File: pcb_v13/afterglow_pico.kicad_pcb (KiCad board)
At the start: 4 copper layers, 69.4 x 88.1 mm, 88 parts, among them J1 USB_B_Micro, J2 Conn_01x02_Male, J4 Conn_02x17_Odd_Even, J5 Conn_02x17_Odd_Even, SW1 SW_Push, U1 NCP1117-3.3_SOT223, U10 74HC257, U11 74HC257, U2 RP2040, U3 SN74LVC245AN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

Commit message: Almost
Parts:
- moved R14 8.14 mm to (162.3, 64.0), turned to 180 degrees
- moved R6 1.13 mm to (155.3, 63.2)
- moved C10 0.53 mm to (159.4, 75.7)
- moved C12 0.32 mm to (154.9, 75.6)
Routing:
- net GND: track 61.7 -> 64.4 mm
- net +3V3: track 211.1 -> 213.5 mm, vias 13 -> 12
- net /QSPI_SS: track 21.4 -> 22.2 mm

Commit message: Preparations
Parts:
- added LOGO: LOGO, pcb_v13:ag_pico_logo_2, F.Cu at (152.8, 69.8)
- moved R35 2.68 mm to (200.2, 113.8)
- moved J5 2.55 mm to (187.3, 133.3)
- moved R33 2.40 mm to (200.2, 116.5)
- moved J2 0.93 mm to (184.8, 140.8)
- turned R21 to 90 degrees
- turned R22 to 90 degrees
- turned R23 to 90 degrees
- turned R24 to 90 degrees
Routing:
- net Vcc: track 305.0 -> 285.1 mm
- net /SOL4: track 0.00 -> 17.7 mm
- net /DIS2: track 0.00 -> 10.3 mm
- net /SOL2: track 4.07 -> 14.4 mm
- net /P33: track 0.00 -> 10.2 mm
- net /SOL1: track 0.00 -> 10.1 mm
- net /ZERO_CROSS: track 0.00 -> 10.0 mm
- net /DIS3: track 0.00 -> 10.0 mm
- net /DIS1: track 0.00 -> 10.0 mm
- net /SOL3: track 7.83 -> 15.6 mm
- net /LCOL: track 0.00 -> 6.67 mm
- net /GPIO3: track 0.00 -> 4.09 mm, vias 0 -> 1
- net /GPIO15: track 0.00 -> 3.28 mm, vias 0 -> 1
- net /GPIO14: track 0.00 -> 3.04 mm, vias 0 -> 1
- net /GPIO2: track 0.00 -> 2.96 mm, vias 0 -> 1
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
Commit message: More preparations
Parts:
- + 5V -: renamed from J2
- renumbered PWR_LED1 to P
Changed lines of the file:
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@@
     (property "Sheetname" "")
     (attr smd)
-    (fp_text reference "R22" (at -0.11 1.225 90) (layer "F.SilkS")
+    (fp_text reference "R22" (at 0.06 -1.05 90) (layer "F.SilkS")
       (effects (font (size 1 1) (thickness 0.15)))
     )
@@
     (property "Sheetname" "")
     (attr smd)
-    (fp_text reference "R21" (at -0.1 1.225 90) (layer "F.SilkS")
+    (fp_text reference "R21" (at 0.025 -1.1 90) (layer "F.SilkS")
       (effects (font (size 1 1) (thickness 0.15)))
     )
@@
     (property "Sheetname" "")
     (attr through_hole)
-    (fp_text reference "J2" (at 1.265 4.125) (layer "F.SilkS")
+    (fp_text reference "+ 5V -" (at 1.075 4.375) (layer "F.SilkS")
       (effects (font (size 1 1) (thickness 0.15)))
     )
@@
     (property "Sheetname" "")
     (attr smd)
-    (fp_text reference "PWR_LED1" (at -2.635 -0.075) (layer "F.SilkS")
+    (fp_text reference "P" (at -2.36 0 180) (layer "F.SilkS")
       (effects (font (size 1 1) (thickness 0.15)))
     )
@@
     (property "Sheetname" "")
     (attr smd)
-    (fp_text reference "C4" (at 2.7 0.025) (layer "F.SilkS")
+    (fp_text reference "C4" (at 2.575 0.025) (layer "F.SilkS")
       (effects (font (size 1 1) (thickness 0.15)))
     )
@@
     (property "Sheetname" "")
     (attr smd)
-    (fp_text reference "U1" (at -0.2 4.35) (layer "F.SilkS")
+    (fp_text reference "U1" (at 0.05 4.425) (layer "F.SilkS")
       (effects (font (size 1 1) (thickness 0.15)))
     )
@@
     (property "Sheetname" "")
     (attr smd)
-    (fp_text reference "D3" (at -2.575 0.15) (layer "F.SilkS")
+    (fp_text reference "D3" (at -2.475 0) (layer "F.SilkS")
       (effects (font (size 1 1) (thickness 0.15)))
     )
@@
     (effects (font (size 0.75 0.75) (thickness 0.1)))
   )
-  (gr_text "1" (at 189.4 135.75) (layer "F.SilkS")
+  (gr_text "1" (at 189.25 133.225) (layer "F.SilkS")
     (effects (font (size 0.75 0.75) (thickness 0.1)))
   )

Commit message: Even more preparations
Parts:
- moved TEST 0.38 mm to (179.1, 61.5)
- renumbered P to PWR, TEST_MODE1 to TEST
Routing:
- net GND: track 64.4 -> 65.2 mm
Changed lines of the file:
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@@
     (property "Sheetname" "")
     (attr smd)
-    (fp_text reference "P" (at -2.36 0 180) (layer "F.SilkS")
+    (fp_text reference "PWR" (at -2.71 -0.05 180) (layer "F.SilkS")
       (effects (font (size 1 1) (thickness 0.15)))
     )
@@
   )
   (footprint "Pin_Headers:Pin_Header_Straight_1x02_Pitch2.54mm" (layer "F.Cu")
-    (at 178.78 61.65 90)
+    (at 179.1 61.45 90)
     (descr "Through hole straight pin header, 1x02, 2.54mm pitch, single row")
     (tags "Through hole pin header THT 1x02 2.54mm single row")
@@
     (property "Sheetname" "")
     (attr through_hole)
-    (fp_text reference "TEST_MODE1" (at -2.875 -0.285) (layer "F.SilkS")
+    (fp_text reference "TEST" (at 0.075 -3.925) (layer "F.SilkS")
       (effects (font (size 1 1) (thickness 0.15)))
     )
@@
     (property "Sheetname" "")
     (attr smd)
-    (fp_text reference "R14" (at 0 2.1 90) (layer "F.SilkS")
+    (fp_text reference "R14" (at 0.375 1.375 180) (layer "F.SilkS")
       (effects (font (size 1 1) (thickness 0.15)))
     )
@@
     (property "Sheetname" "")
     (attr smd)
-    (fp_text reference "J1" (at 0 -3.1125) (layer "F.SilkS")
+    (fp_text reference "J1" (at -3.475 -3.535) (layer "F.SilkS")
       (effects (font (size 1 1) (thickness 0.15)))
     )
@@
   (segment (start 144.08 113) (end 144.08 114.145) (width 0.2) (layer "F.Cu") (net 1))
   (segment (start 154.925 75.145) (end 154.925 74.3) (width 0.2) (layer "F.Cu") (net 1))
+  (segment (start 200.75 129.15) (end 200.75 128.875) (width 0.2) (layer "F.Cu") (net 1))
   (segment (start 139.6625 95.1875) (end 139.65 95.2) (width 0.2) (layer "F.Cu") (net 1))
   (segment (start 177.405 109.72) (end 177.225 109.9) (width 0.2) (layer "F.Cu") (net 1))
@@
   (segment (start 147.225 78.32) (end 147.225 77.15) (width 0.2) (layer "F.Cu") (net 1))
   (segment (start 146.4625 107.075) (end 145.1 107.075) (width 0.2) (layer "F.Cu") (net 1))
+  (segment (start 200.75 128.875) (end 201.725 127.9) (width 0.2) (layer "F.Cu") (net 1))
   (segment (start 149.545474 79.3755) (end 149.225 79.3755) (width 0.2) (layer "F.Cu") (net 1))
   (segment (start 161.475 97.57) (end 160.63 97.57) (width 0.2) (layer "F.Cu") (net 1))
@@
   (segment (start 178.25 109.72) (end 177.405 109.72) (width 0.2) (layer "F.Cu") (net 1))
   (segment (start 161.15 88.68) (end 159.85 88.68) (width 0.2) (layer "F.Cu") (net 1))
-  (segment (start 201.5 129.15) (end 201.525 129.125) (width 0.2) (layer "F.Cu") (net 1))
   (segment (start 200.6 132.95) (end 199.725 132.95) (width 0.5) (layer "F.Cu") (net 1))
   (segment (start 154.925 74.3) (end 154.95 74.275) (width 0.2) (layer "F.Cu") (net 1))
   (segment (start 160.0375 107.075) (end 158.725 107.075) (width 0.2) (layer "F.Cu") (net 1))
-  (segment (start 200.75 129.15) (end 201.5 129.15) (width 0.2) (layer "F.Cu") (net 1))
   (segment (start 157.655 113.995) (end 157.65 114) (width 0.2) (layer "F.Cu") (net 1))
   (segment (start 157.655 113) (end 157.655 113.995) (width 0.2) (layer "F.Cu") (net 1))
@@
   (via (at 145.1 107.075) (size 0.6) (drill 0.35) (layers "F.Cu" "B.Cu") (net 1))
   (via (at 161.725 67.975) (size 0.6) (drill 0.35) (layers "F.Cu" "B.Cu") (net 1))
+  (via (at 201.725 127.9) (size 0.6) (drill 0.35) (layers "F.Cu" "B.Cu") (net 1))
   (via (at 160.625 97.575) (size 0.6) (drill 0.35) (layers "F.Cu" "B.Cu") (net 1))
   (via (at 165.575 77.725) (size 0.6) (drill 0.35) (layers "F.Cu" "B.Cu") (net 1))
@@
   (via (at 167.75 108.2) (size 0.6) (drill 0.35) (layers "F.Cu" "B.Cu") (net 1))
   (via (at 159.375 74.25) (size 0.6) (drill 0.35) (layers "F.Cu" "B.Cu") (net 1))
-  (via (at 201.525 129.125) (size 0.6) (drill 0.35) (layers "F.Cu" "B.Cu") (net 1))
   (via (at 158.7 107.1) (size 0.6) (drill 0.35) (layers "F.Cu" "B.Cu") (net 1))
   (via (at 147.225 83.275) (size 0.6) (drill 0.35) (layers "F.Cu" "B.Cu") (net 1))
@@
   (segment (start 191.3 137.625) (end 193.4 139.725) (width 0.5) (layer "F.Cu") (net 41))
   (segment (start 193.4 139.725) (end 193.4 141.7) (width 0.5) (layer "F.Cu") (net 41))
+  (segment (start 174.325 64.125) (end 174.375 64.075) (width 0.5) (layer "F.Cu") (net 42))
   (segment (start 193.4 136.425) (end 193.375 136.4) (width 0.5) (layer "F.Cu") (net 42))
   (segment (start 169.475 63.45) (end 169.475 62.5025) (width 0.5) (layer "F.Cu") (net 42))
   (segment (start 170.15 64.125) (end 169.475 63.45) (width 0.5) (layer "F.Cu") (net 42))
+  (segment (start 170.15 64.125) (end 174.325 64.125) (width 0.5) (layer "F.Cu") (net 42))
   (segment (start 193.4 137.625) (end 193.4 136.425) (width 0.5) (layer "F.Cu") (net 42))
-  (via (at 170.15 64.125) (size 0.6) (drill 0.35) (layers "F.Cu" "B.Cu") (net 42))
+  (via (at 174.375 64.075) (size 0.6) (drill 0.35) (layers "F.Cu" "B.Cu") (net 42))
   (via (at 193.375 136.4) (size 0.6) (drill 0.35) (layers "F.Cu" "B.Cu") (net 42))
-  (segment (start 187.325 89.8) (end 185.925 88.4) (width 0.5) (layer "In2.Cu") (net 42))
-  (segment (start 191.125 134.15) (end 191.125 92.375) (width 0.5) (layer "In2.Cu") (net 42))
-  (segment (start 185.925 64.625) (end 185.425 64.125) (width 0.5) (layer "In2.Cu") (net 42))
-  (segment (start 188.55 89.8) (end 187.325 89.8) (width 0.5) (layer "In2.Cu") (net 42))
-  (segment (start 185.925 88.4) (end 185.925 64.625) (width 0.5) (layer "In2.Cu") (net 42))
-  (segment (start 185.425 64.125) (end 170.15 64.125) (width 0.5) (layer "In2.Cu") (net 42))
-  (segment (start 193.375 136.4) (end 191.125 134.15) (width 0.5) (layer "In2.Cu") (net 42))
-  (segment (start 191.125 92.375) (end 188.55 89.8) (width 0.5) (layer "In2.Cu") (net 42))
+  (segment (start 185.925 64.625) (end 185.925 88.4) (width 0.5) (layer "In2.Cu") (net 42))
+  (segment (start 191.125 134.15) (end 193.375 136.4) (width 0.5) (layer "In2.Cu") (net 42))
+  (segment (start 174.375 64.075) (end 185.375 64.075) (width 0.5) (layer "In2.Cu") (net 42))
+  (segment (start 188.55 89.8) (end 191.125 92.375) (width 0.5) (layer "In2.Cu") (net 42))
+  (segment (start 187.325 89.8) (end 188.55 89.8) (width 0.5) (layer "In2.Cu") (net 42))
+  (segment (start 185.925 88.4) (end 187.325 89.8) (width 0.5) (layer "In2.Cu") (net 42))
+  (segment (start 185.375 64.075) (end 185.925 64.625) (width 0.5) (layer "In2.Cu") (net 42))
+  (segment (start 191.125 92.375) (end 191.125 134.15) (width 0.5) (layer "In2.Cu") (net 42))
   (segment (start 168.825 62.5025) (end 168.825 63.8) (width 0.5) (layer "F.Cu") (net 45))
   (segment (start 169 63.975) (end 169 64.65) (width 0.5) (layer "F.Cu") (net 45))
@@
       )
     )
+  )
+  (zone (net 0) (net_name "") (layer "F.Cu") (hatch edge 0.508)
+    (connect_pads (clearance 0))
+    (min_thickness 0.254)
+    (keepout (tracks not_allowed) (vias not_allowed) (pads not_allowed) (copperpour allowed) (footprints allowed))
+    (fill (thermal_gap 0.508) (thermal_bridge_width 0.508))
+    (polygon
+      (pts
+        (xy 169.775 81.825)
+        (xy 167.35 84.25)
+        (xy 165.175 84.25)
+        (xy 165.175 81.775)
+        (xy 166.25 81.775)
+        (xy 167.25 80.775)
+        (xy 167.25 63.475)
+        (xy 169.775 63.475)
+      )
+    )

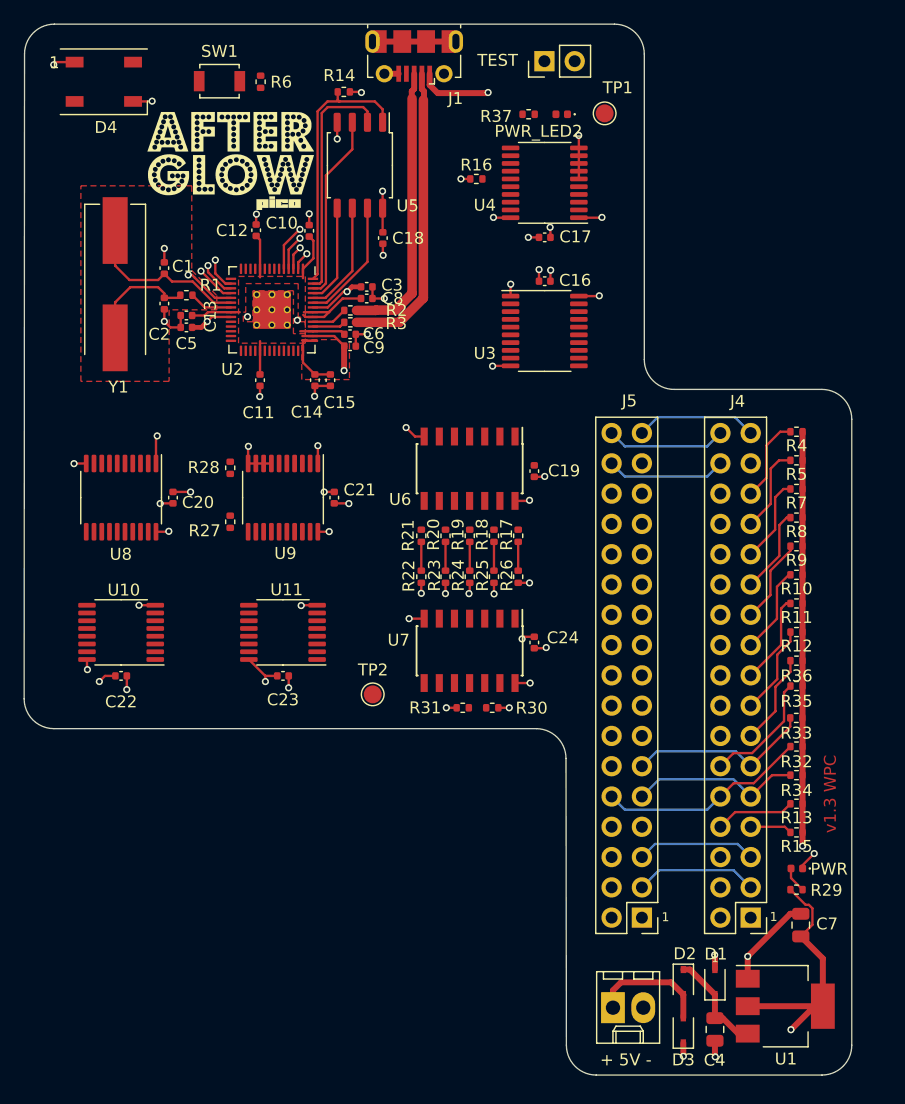
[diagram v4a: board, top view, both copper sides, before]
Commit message: Forgot a resistor
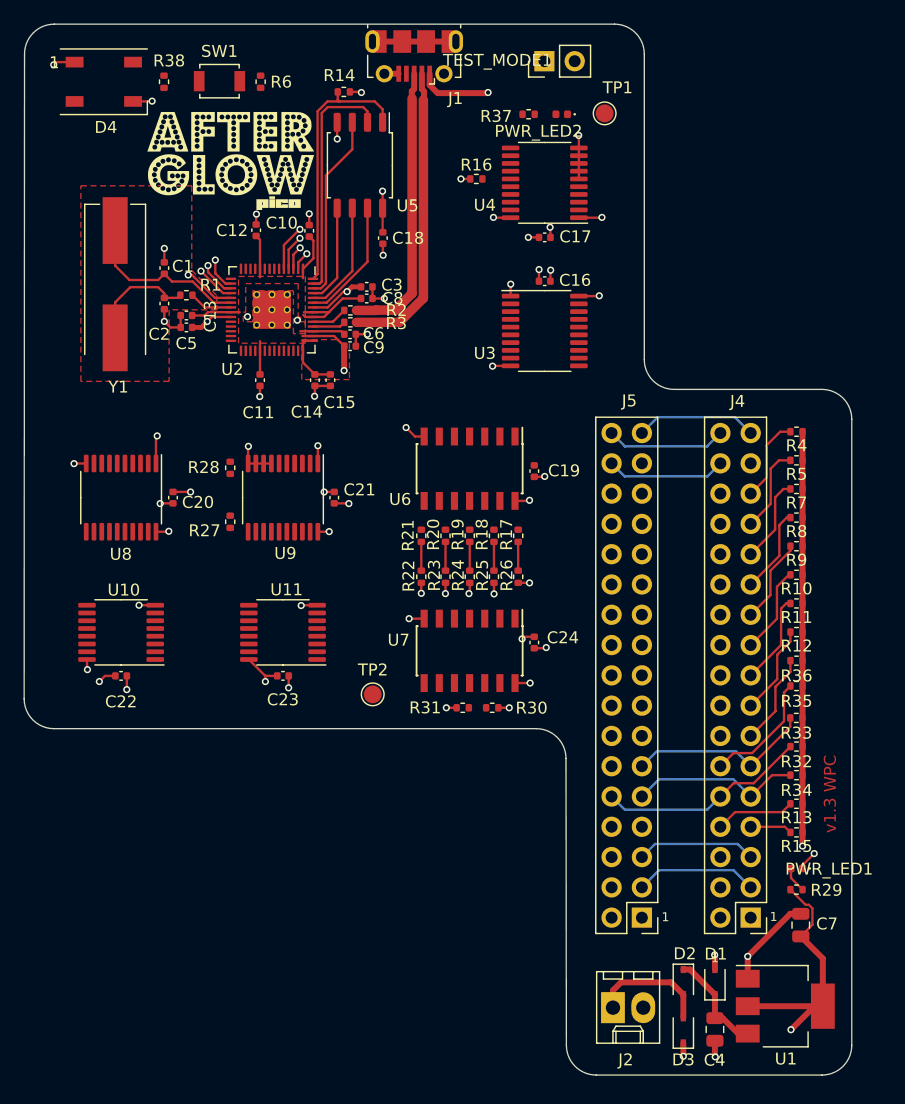
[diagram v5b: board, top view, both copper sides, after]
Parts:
- added R38: 220, Resistor_SMD:R_0402_1005Metric, F.Cu at (147.2, 63.2)
- J2: renamed from + 5V -
- R29: value 180 -> 1k
- renumbered PWR to PWR_LED1, TEST to TEST_MODE1
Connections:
- D4 pad 4: /PICO_WS2812 -> Net-(D4-Pad4)

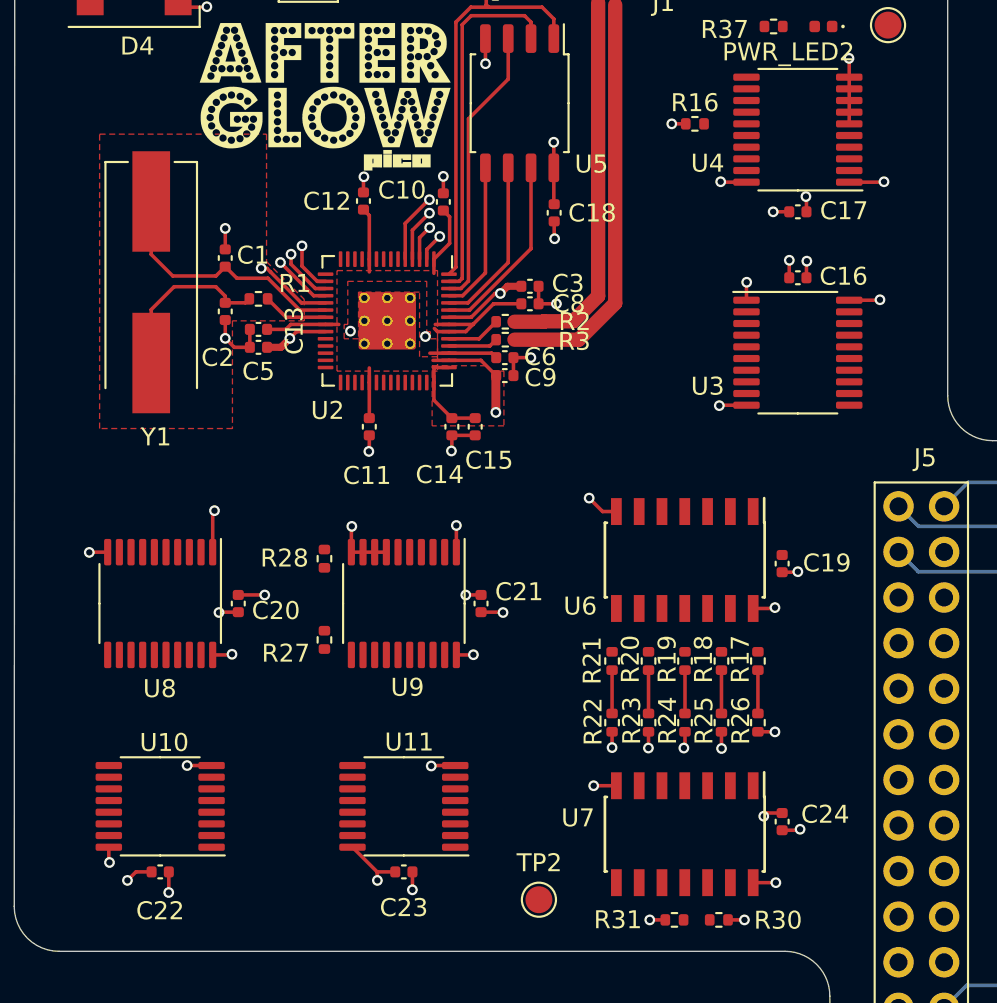
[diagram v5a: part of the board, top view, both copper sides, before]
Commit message: Avoid vias on tracks
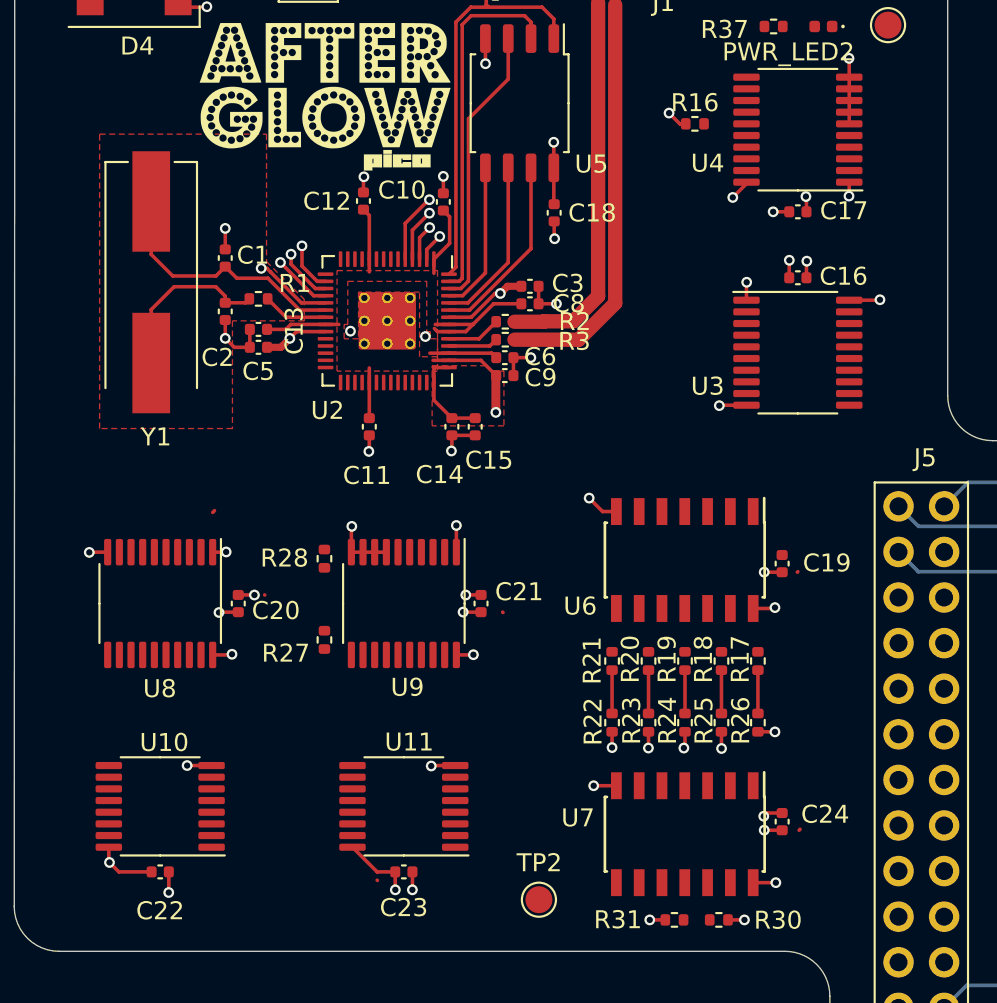
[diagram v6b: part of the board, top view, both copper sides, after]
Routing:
- net Vcc: track 285.1 -> 294.3 mm, vias 21 -> 20
- net +3V3: track 215.0 -> 215.6 mm
